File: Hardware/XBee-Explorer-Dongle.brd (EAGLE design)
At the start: 40.6 x 27.9 mm, 38 parts, among them U2 XBEE-1B3, U3 MIC5219 3.3V, U4 FT231XS

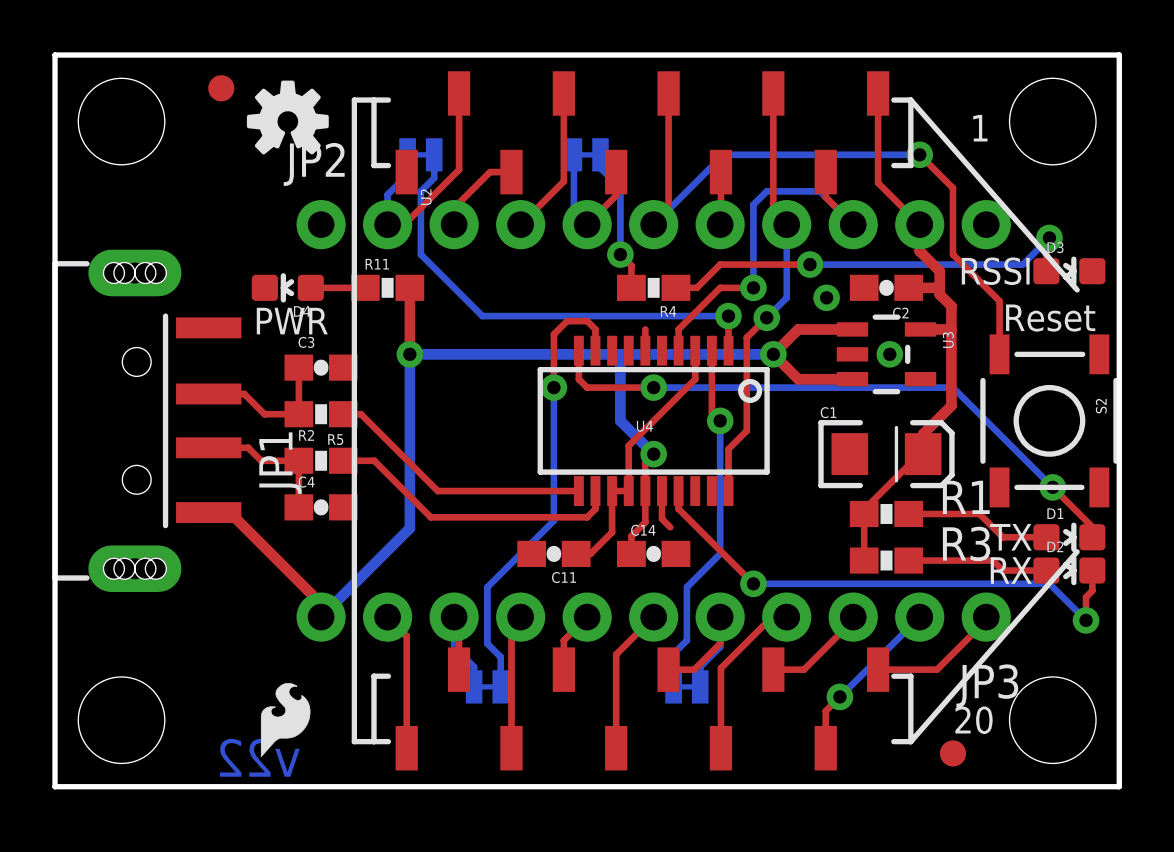
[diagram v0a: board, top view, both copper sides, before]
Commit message: Upd to usb pth, 0603, sch changes
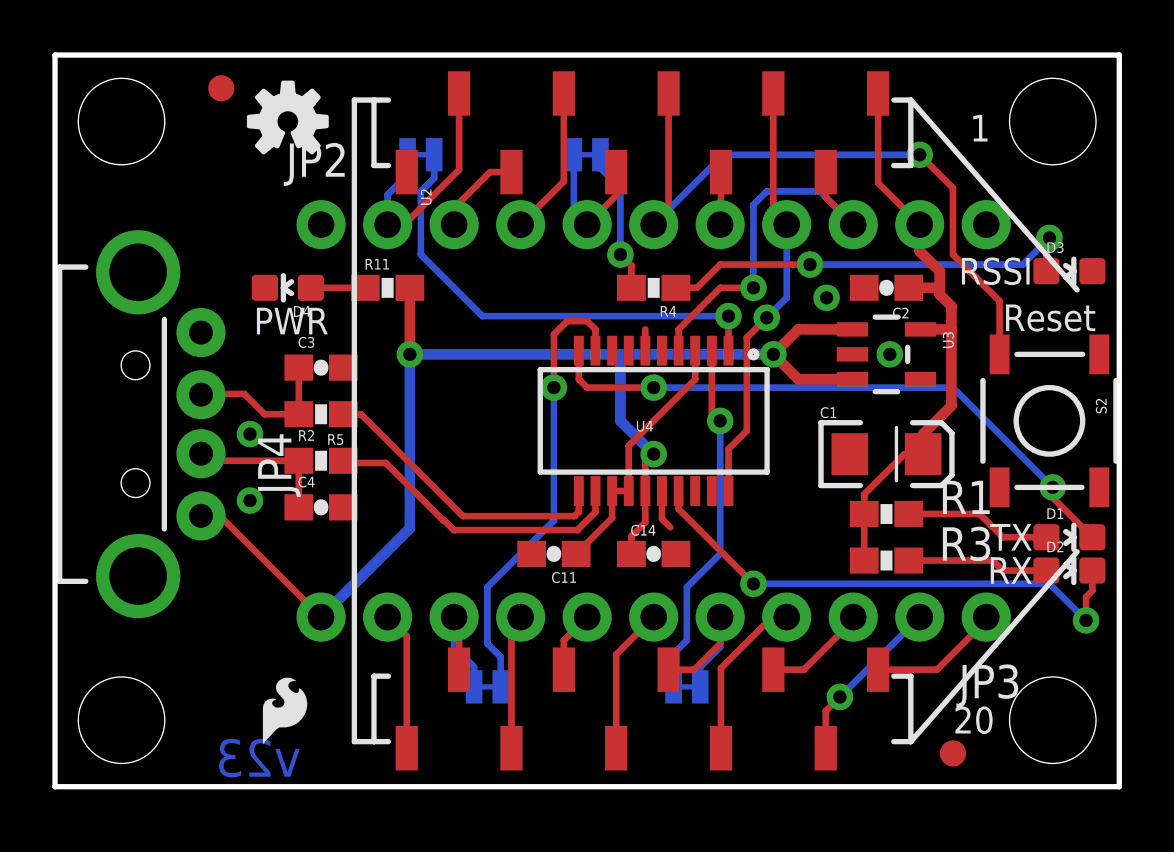
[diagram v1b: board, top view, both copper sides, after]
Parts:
- removed JP1: USBA-SMD-MALE-LOCKING, SparkFun-Connectors:USB-A-SMT-MALE-LOCKING
- removed U$1: LOGO-SFESK, SparkFun:SFE-LOGO-FLAME
- removed U$4: LOGO-SFENEW, SparkFun:SFE-NEW-WEBLOGO
- removed U$8: OSHW-LOGOS, SparkFun:OSHW-LOGO-S
- added JP4: USB-A-H, SparkFun-Connectors:USB-A-H
- added LOGO1: SFE_LOGO_FLAME.1_INCH, SparkFun-Aesthetics:SFE_LOGO_FLAME_.1
- added LOGO2: SFE_LOGO_NAME.2_INCH, SparkFun-Aesthetics:SFE_LOGO_NAME_.2
- C1: device SparkFun:EIA3216 -> SparkFun-Capacitors:EIA3216
- C2, C3, C4: device SparkFun:0603-CAP -> SparkFun-Capacitors:0603-CAP
- R1, R11, R2, R3, R4, R5: device SparkFun:0603-RES -> SparkFun-Resistors:0603-RES
- U3: device SparkFun:SOT23-5 -> SparkFun-PowerIC:SOT23-5
- U4: value FT231XS -> FTS31XS-U
- moved FRAME1 16.6 mm to (-10.2, -10.2)
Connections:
- net 5V: now also JP4.VBUS; no longer JP1.VBUS1
- net GND: now also JP4.GND; no longer JP1.GND1
- net N$3: now also JP4.D-; no longer JP1.D-1
- net N$6: now also JP4.D+; no longer JP1.D+1
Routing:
- net N$7: track 10.2 -> 11.5 mm
- net 3.3V: track 22.8 -> 23.3 mm
- net GND: vias 2 -> 4
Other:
- board text added: "Revised by: Patrick Alberts"
- board text added: "Xbee Dongle"
- board text added: "v23"
- board text removed: "v22"

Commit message: QC checklist items complete.
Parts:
- C11, C14: device SparkFun:0603-CAP -> SparkFun-Capacitors:0603-CAP
- D1: value RED -> GREEN
- D2: value GREEN -> Yellow
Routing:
- net 3V-INT: track 10.0 -> 10.9 mm
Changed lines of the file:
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@@
 </autorouter>
 <elements>
-<element name="C11" library="SparkFun" package="0603-CAP" value="0.1uF" x="19.05" y="8.89" smashed="yes" rot="R180">
+<element name="C11" library="SparkFun-Capacitors" package="0603-CAP" value="0.1uF" x="19.05" y="8.89" smashed="yes" rot="R180">
 <attribute name="NAME" x="19.939" y="8.1915" size="0.4064" layer="25" rot="R180"/>
-<attribute name="VALUE" x="16.1925" y="8.763" size="0.4064" layer="27"/>
+<attribute name="VALUE" value="0.1uF" x="16.1925" y="8.763" size="0.4064" layer="27"/>
+<attribute name="PROD_ID" value="CAP-00810" x="19.05" y="8.89" size="1.778" layer="27" rot="R180" display="off"/>
 </element>
 <element name="R11" library="SparkFun-Resistors" package="0603-RES" value="1K" x="12.7" y="19.05" smashed="yes">
@@
 <attribute name="PROD_ID" value="RES-07856" x="12.7" y="19.05" size="1.778" layer="27" display="off"/>
 </element>
-<element name="C14" library="SparkFun" package="0603-CAP" value="0.1uF" x="22.86" y="8.89" smashed="yes">
+<element name="C14" library="SparkFun-Capacitors" package="0603-CAP" value="0.1uF" x="22.86" y="8.89" smashed="yes">
 <attribute name="NAME" x="21.971" y="9.5885" size="0.4064" layer="25"/>
-<attribute name="VALUE" x="19.8755" y="8.636" size="0.4064" layer="27"/>
+<attribute name="VALUE" value="0.1uF" x="19.8755" y="8.636" size="0.4064" layer="27"/>
+<attribute name="PROD_ID" value="CAP-00810" x="22.86" y="8.89" size="1.778" layer="27" display="off"/>
 </element>
 <element name="R1" library="SparkFun-Resistors" package="0603-RES" value="1K" x="31.75" y="10.414" smashed="yes">
@@
 <element name="SJ3" library="SparkFun-Passives" package="SJ_2S-TRACE" value="RSSI" x="16.51" y="3.81" rot="MR0"/>
 <element name="SJ4" library="SparkFun-Passives" package="SJ_2S-TRACE" value="RSSI" x="13.97" y="24.13" rot="MR0"/>
-<element name="D1" library="SparkFun-LED" package="LED-0603" value="RED" x="38.735" y="9.525" rot="R270">
-<attribute name="PROD_ID" value="DIO-00819" x="38.735" y="9.525" size="1.778" layer="27" font="vector" ratio="15" rot="R270" display="off"/>
-</element>
-<element name="D2" library="SparkFun-LED" package="LED-0603" value="GREEN" x="38.735" y="8.255" rot="R270">
-<attribute name="PROD_ID" value="DIO-00821" x="38.735" y="8.255" size="1.778" layer="27" font="vector" ratio="15" rot="R270" display="off"/>
+<element name="D1" library="SparkFun-LED" package="LED-0603" value="GREEN" x="38.735" y="9.525" rot="R270">
+<attribute name="PROD_ID" value="DIO-00821" x="38.735" y="9.525" size="1.778" layer="27" font="vector" ratio="15" rot="R270" display="off"/>
+</element>
+<element name="D2" library="SparkFun-LED" package="LED-0603" value="Yellow" x="38.735" y="8.255" rot="R270">
+<attribute name="PROD_ID" value="DIO-09003" x="38.735" y="8.255" size="1.778" layer="27" font="vector" ratio="15" rot="R270" display="off"/>
 </element>
 <element name="D3" library="SparkFun-LED" package="LED-0603" value="GREEN" x="38.735" y="19.685" rot="R270">
@@
 <contactref element="U4" pad="3"/>
 <contactref element="U4" pad="13"/>
-<wire x1="21.9075" y1="11.2903" x2="21.2725" y2="11.2903" width="0.254" layer="1"/>
 <wire x1="21.9075" y1="11.2903" x2="21.9075" y2="13.0175" width="0.254" layer="1"/>
 <wire x1="24.4475" y1="16.6497" x2="24.4475" y2="15.5575" width="0.254" layer="1"/>
 <wire x1="24.4475" y1="15.5575" x2="21.9075" y2="13.0175" width="0.254" layer="1"/>
-<wire x1="21.2725" y1="11.2903" x2="21.2725" y2="10.2625" width="0.254" layer="1"/>
+<wire x1="21.2725" y1="11.2903" x2="21.2725" y2="10.398759375" width="0.254" layer="1"/>
+<wire x1="21.2725" y1="10.398759375" x2="21.2725" y2="10.2625" width="0.254" layer="1"/>
 <wire x1="21.2725" y1="10.2625" x2="19.9" y2="8.89" width="0.254" layer="1"/>
+<wire x1="21.9075" y1="11.2903" x2="21.9075" y2="10.482578125" width="0.254" layer="1"/>
+<wire x1="21.9075" y1="10.482578125" x2="21.846540625" y2="10.42161875" width="0.254" layer="1"/>
+<wire x1="21.846540625" y1="10.42161875" x2="21.295359375" y2="10.42161875" width="0.254" layer="1"/>
+<wire x1="21.295359375" y1="10.42161875" x2="21.2725" y2="10.398759375" width="0.254" layer="1"/>
 </signal>
 <signal name="N$3">
@@
 <wire x1="20.6375" y1="11.2903" x2="20.6375" y2="10.4902" width="0.254" layer="1"/>
 <wire x1="20.6375" y1="10.4902" x2="19.94661875" y2="9.79931875" width="0.254" layer="1"/>
-<wire x1="19.94661875" y1="9.79931875" x2="15.2273" y2="9.79931875" width="0.254" layer="1"/>
-<wire x1="15.2273" y1="9.79931875" x2="14.856459375" y2="10.170159375" width="0.254" layer="1"/>
-<wire x1="14.856459375" y1="10.170159375" x2="14.82598125" y2="10.170159375" width="0.254" layer="1"/>
-<wire x1="14.82598125" y1="10.170159375" x2="12.633959375" y2="12.36218125" width="0.254" layer="1"/>
-<wire x1="12.633959375" y1="12.36218125" x2="11.09381875" y2="12.36218125" width="0.254" layer="1"/>
+<wire x1="19.94661875" y1="9.79931875" x2="14.73961875" y2="9.79931875" width="0.254" layer="1"/>
 <wire x1="11.09381875" y1="12.36218125" x2="11.01" y2="12.446" width="0.254" layer="1"/>
+<wire x1="14.73961875" y1="9.79931875" x2="12.09801875" y2="12.44091875" width="0.254" layer="1"/>
+<wire x1="12.09801875" y1="12.44091875" x2="11.01508125" y2="12.44091875" width="0.254" layer="1"/>
+<wire x1="11.01508125" y1="12.44091875" x2="11.01" y2="12.446" width="0.254" layer="1"/>
 </signal>
 <signal name="N$6">
@@
 <contactref element="R4" pad="2"/>
 <contactref element="SJ1" pad="2"/>
-<wire x1="20.828" y1="24.13" x2="20.828" y2="23.622" width="0.254" layer="16"/>
-<wire x1="20.828" y1="23.622" x2="21.59" y2="22.86" width="0.254" layer="16"/>
-<wire x1="21.59" y1="22.86" x2="21.59" y2="20.32" width="0.254" layer="16"/>
 <via x="21.59" y="20.32" extent="1-16" drill="0.508"/>
 <wire x1="21.59" y1="20.32" x2="22.01" y2="19.9" width="0.254" layer="1"/>
 <wire x1="22.01" y1="19.05" x2="22.01" y2="19.9" width="0.254" layer="1"/>
+<wire x1="21.59" y1="20.32" x2="21.59" y2="22.458678125" width="0.254" layer="16"/>
+<wire x1="21.59" y1="22.458678125" x2="20.825459375" y2="23.22321875" width="0.254" layer="16"/>
+<wire x1="20.825459375" y1="23.22321875" x2="20.825459375" y2="24.127459375" width="0.254" layer="16"/>
+<wire x1="20.825459375" y1="24.127459375" x2="20.828" y2="24.13" width="0.254" layer="16"/>
 </signal>
 <signal name="RTS_XBEE">
